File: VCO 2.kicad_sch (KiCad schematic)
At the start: 99 parts, among them J1 OUT 1x4s, J16 OCT_SW 1x7s, J18 CV 1x6s, J8 CTRL 1x8s, J85 Eurorack 2x8hs, J9 IN 1x6s, Q1 2N3904, Q2 2N3904, U1 CEM3340, U2 TL074, U3 TL074, U4 LM336Z-2.5/LFT3

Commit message: Moved LED to control board.
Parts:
- removed D1: LED, symbol Device:LED
- added J20: LED 1x2s, symbol Connector:Conn_01x02_Socket
- R51: value 470R -> 470R/520R
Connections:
- net +12V: no longer C18.1, C20.1, R73.1
- net at R51.1: now also J20.2 (Pin_2)
- new net: C18.1, C20.1, J20.1 (Pin_1), R73.1
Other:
- note added: "3.1V/2.1V"
- note added: "Based on the Thomas Henry sine wave shaper"
- note added: "Needs to be precise"
- note removed: "This is the sine wave generator"
- moved on the sheet: C4, C5, C7, C8, R51, TP22, U2E, U3E

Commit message: Updated TP names
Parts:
- TP2: value SQR -> Sqr
- TP3: value SAW -> Saw
- TP4: value TRI -> Tri
- TP5: value SIN -> Sine
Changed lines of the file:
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@@
 			)
 		)
-		(property "Value" "SAW"
+		(property "Value" "Saw"
 			(at 146.05 51.3079 0)
 			(effects
@@
 			)
 		)
-		(property "Value" "SIN"
+		(property "Value" "Sine"
 			(at 308.61 49.0221 0)
 			(effects
@@
 			)
 		)
-		(property "Value" "TRI"
+		(property "Value" "Tri"
 			(at 147.32 80.5179 0)
 			(effects
@@
 			)
 		)
-		(property "Value" "SQR"
+		(property "Value" "Sqr"
 			(at 146.05 27.1779 0)
 			(effects

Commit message: Added fp and moved controls
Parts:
- C1: value 10nF -> 10nF f; footprint Capacitor_THT:C_Disc_D4.7mm_W2.5mm_P5.00mm -> Capacitor_THT:C_Rect_L7.2mm_W2.5mm_P5.00mm
- C10, C11: value 100nF -> 100nF f; footprint Capacitor_THT:C_Disc_D4.7mm_W2.5mm_P5.00mm -> Capacitor_THT:C_Rect_L7.2mm_W2.5mm_P5.00mm
- C12, C20, C21, C4, C5, C7, C8: value 0.1μF -> 0.1μF c
- C13: value 1nF -> 1nF f; footprint (none) -> Capacitor_THT:C_Rect_L7.2mm_W2.5mm_P5.00mm
- C14: value 10uF -> 10uF c; footprint (none) -> Capacitor_THT:C_Disc_D4.7mm_W2.5mm_P5.00mm
- C18, C19: value 47μF -> 47μF e
- C2: value 10μF -> 10μF c
- C3: value 100nF -> 100nF c
- C6: value 1000pF -> 1000pF f; footprint Capacitor_THT:C_Disc_D4.7mm_W2.5mm_P5.00mm -> Capacitor_THT:C_Rect_L7.2mm_W2.5mm_P5.00mm
- C9: value 1nF -> 1nF f; footprint Capacitor_THT:C_Disc_D4.7mm_W2.5mm_P5.00mm -> Capacitor_THT:C_Rect_L7.2mm_W2.5mm_P5.00mm
- H1, H2, H3, H4: value ~ -> (none)
- J20: footprint (none) -> Connector_PinSocket_2.54mm:PinSocket_1x02_P2.54mm_Vertical
- J8: footprint (none) -> Connector_PinSocket_2.54mm:PinSocket_1x08_P2.54mm_Vertical
- R17, R43, R44, R45, R46, R47, R48, R49, R50, R51: footprint (none) -> Resistor_THT:R_Axial_DIN0204_L3.6mm_D1.6mm_P7.62mm_Horizontal
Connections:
- net +12V: now also C18.1, C20.1, J20.1 (Pin_1), R73.1
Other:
- added sheet Front Panel (front_panel.kicad_sch)
- sheet Controls: file untitled.kicad_sch -> controls.kicad_sch

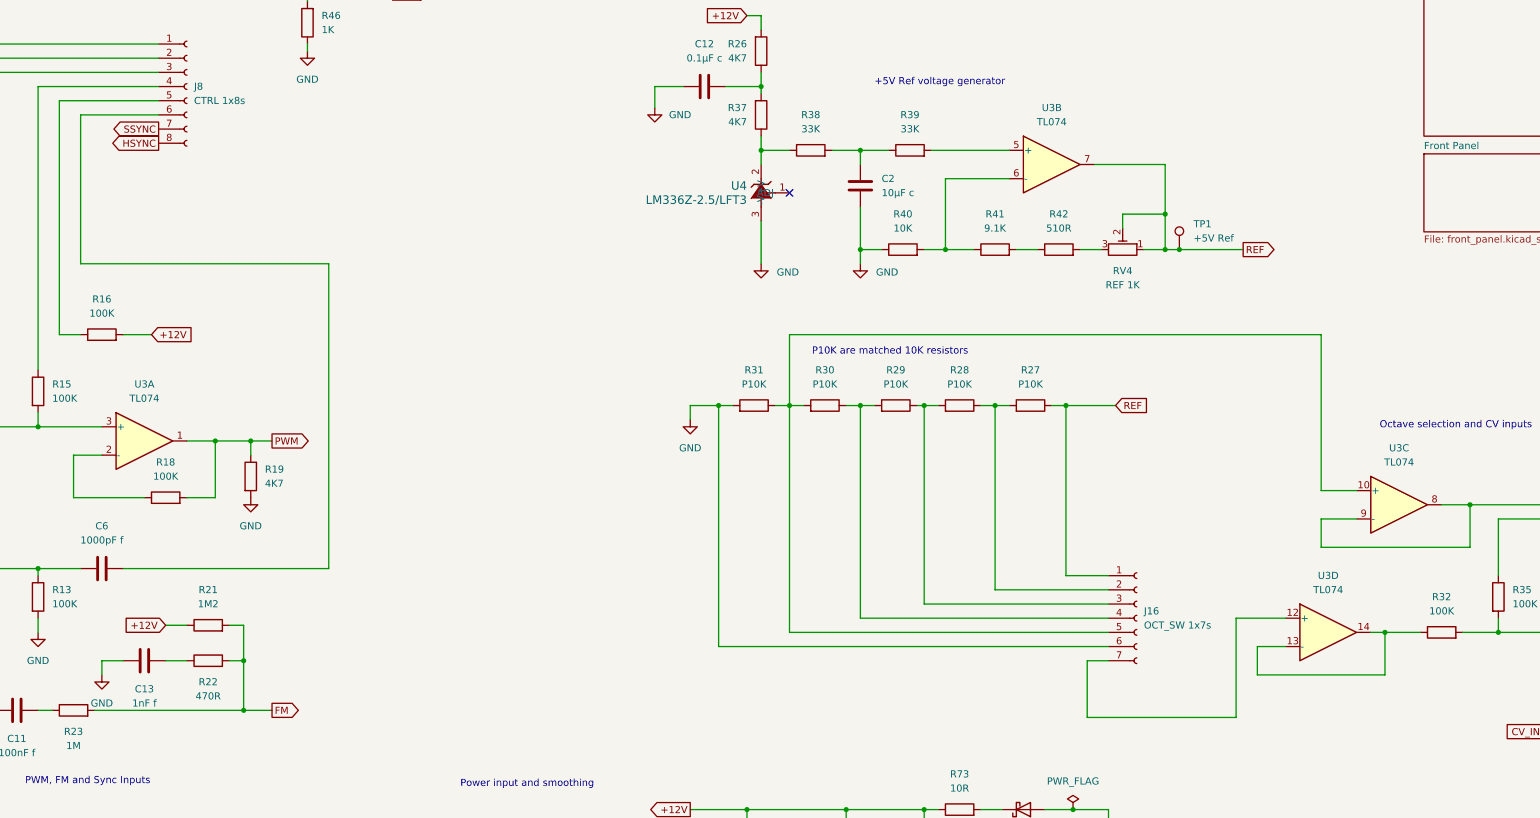
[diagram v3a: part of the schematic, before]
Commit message: Designed PCB and generated JLCPCB files
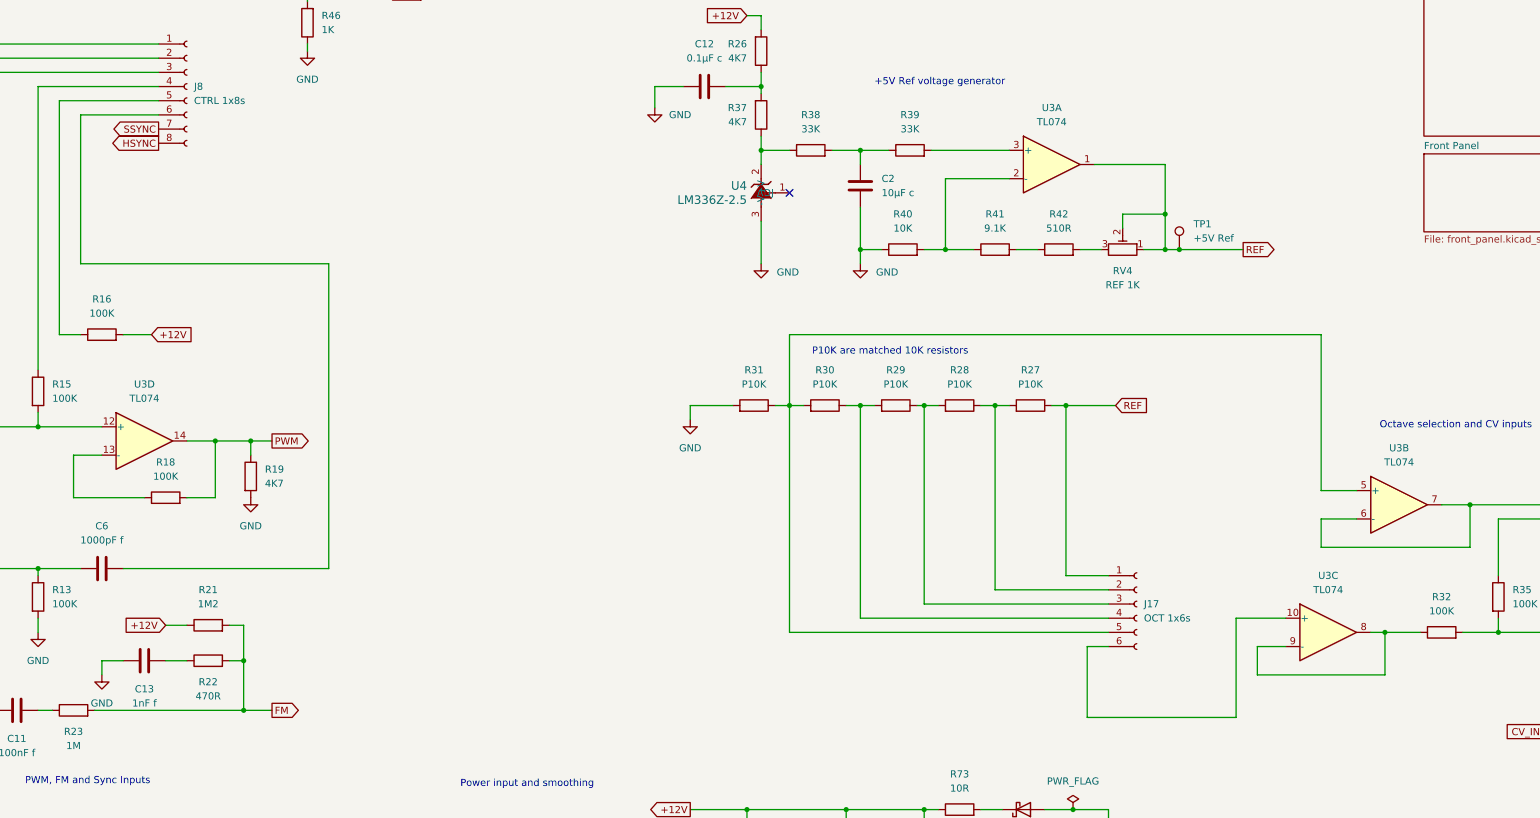
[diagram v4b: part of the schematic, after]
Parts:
- removed J16: OCT_SW 1x7s, Connector_PinSocket_2.54mm:PinSocket_1x07_P2.54mm_Vertical, symbol Connector:Conn_01x07_Socket
- added J17: OCT 1x6s, Connector_PinSocket_2.54mm:PinSocket_1x06_P2.54mm_Vertical, symbol Connector:Conn_01x06_Socket
- Q1, Q2: footprint Package_TO_SOT_THT:TO-92_Inline -> Package_TO_SOT_THT:TO-92_Inline_Wide
- R10, R11, R12, R13, R14, R15, R16, R17, R18, R19, R2, R20, R21, R24, R26, R27, R28, R29, R30, R31, R33, R34, R35, R36, R37, R38, R39, R4, R40, R41, R42, R43, R44, R45, R46, R47, R49, R5, R50, R51, R7, R73, R74, R8, R9: footprint Resistor_THT:R_Axial_DIN0204_L3.6mm_D1.6mm_P7.62mm_Horizontal -> Resistor_THT:R_Axial_DIN0204_L3.6mm_D1.6mm_P2.54mm_Vertical
- U4: value LM336Z-2.5/LFT3 -> LM336Z-2.5
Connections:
- net PWM: now also U3.14; no longer U3.1
- net REF: now also U3.1, J17.1 (Pin_1); no longer U3.7
- net at R39.2: now also U3.3 (+); no longer U3.5 (+)
- net at R40.2, R41.1: now also U3.2 (-); no longer U3.6 (-)
- net at R30.2, R31.1: now also U3.5 (+), J17.5 (Pin_5); no longer U3.10 (+)
- net at U3.8, U3.9 (-): now also R32.1; no longer J18.1 (Pin_1)
- net at R28.2, R29.1: now also J17.3 (Pin_3)
- net at R29.2, R30.1: now also J17.4 (Pin_4)
- net at R27.2, R28.1: now also J17.2 (Pin_2)
- net at U3.12 (+): now also R14.2, R15.2
- net at R18.1: now also U3.13 (-); no longer U3.2 (-)
- new net: J18.1 (Pin_1), U3.6 (-), U3.7
- new net: J17.6 (Pin_6), U3.10 (+)

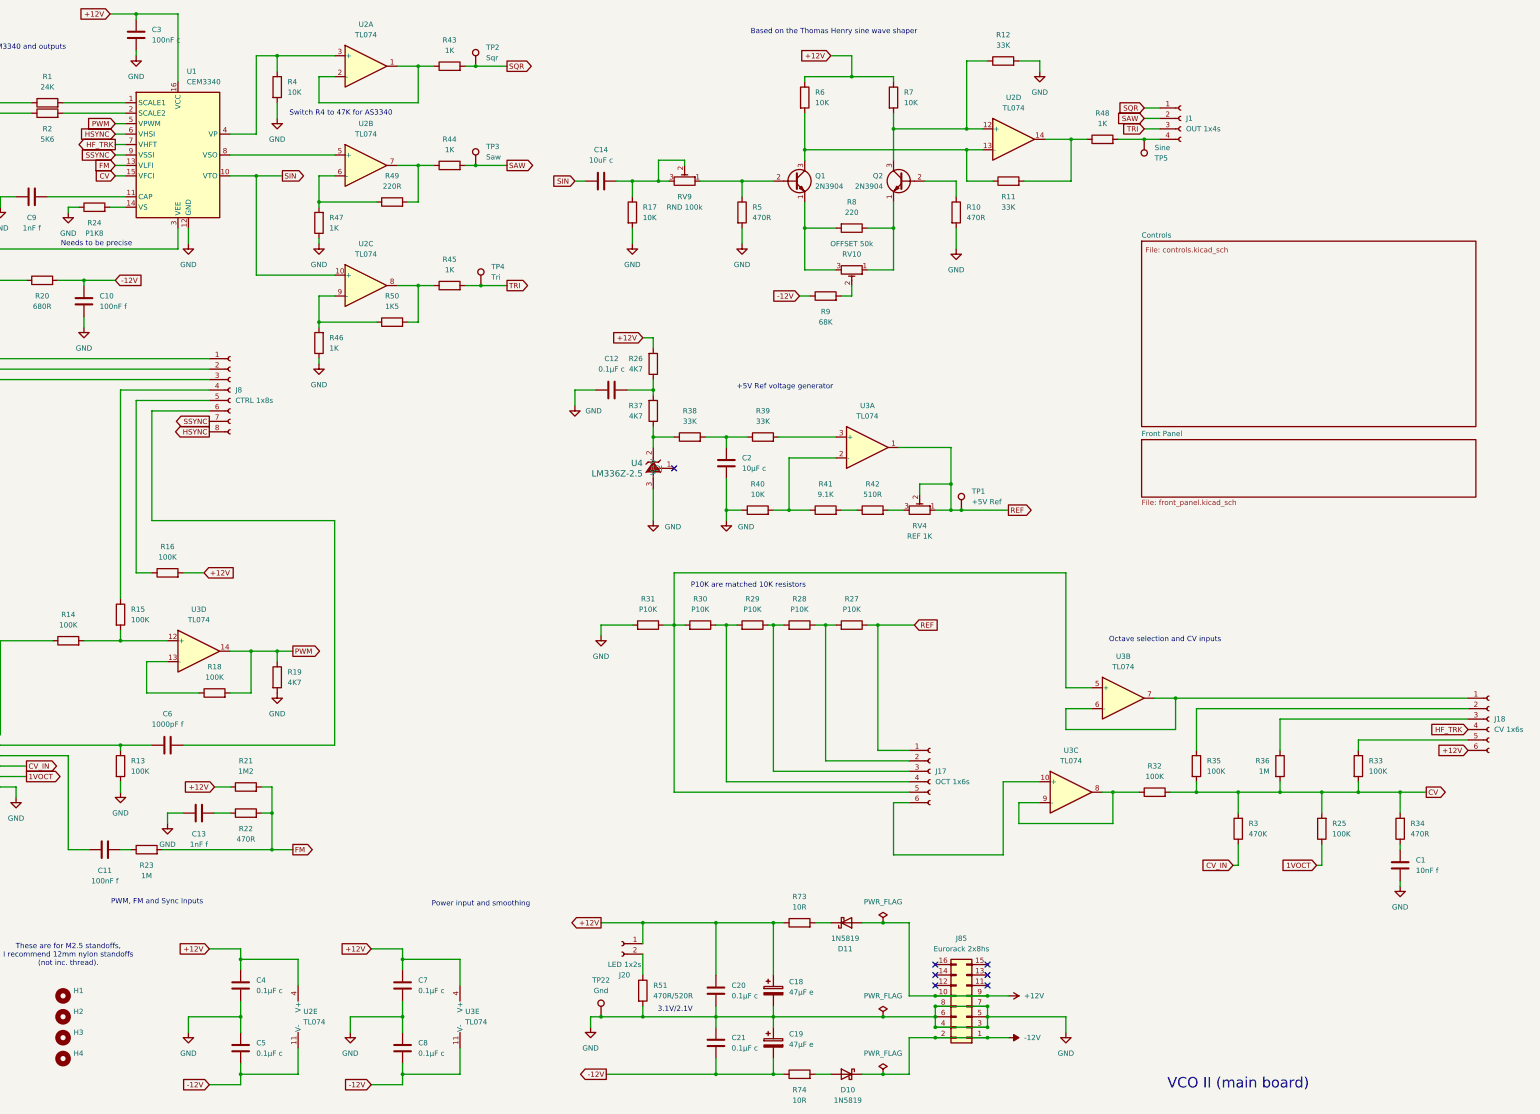
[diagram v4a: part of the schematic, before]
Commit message: Fixed switches, added new FPs and symbols.
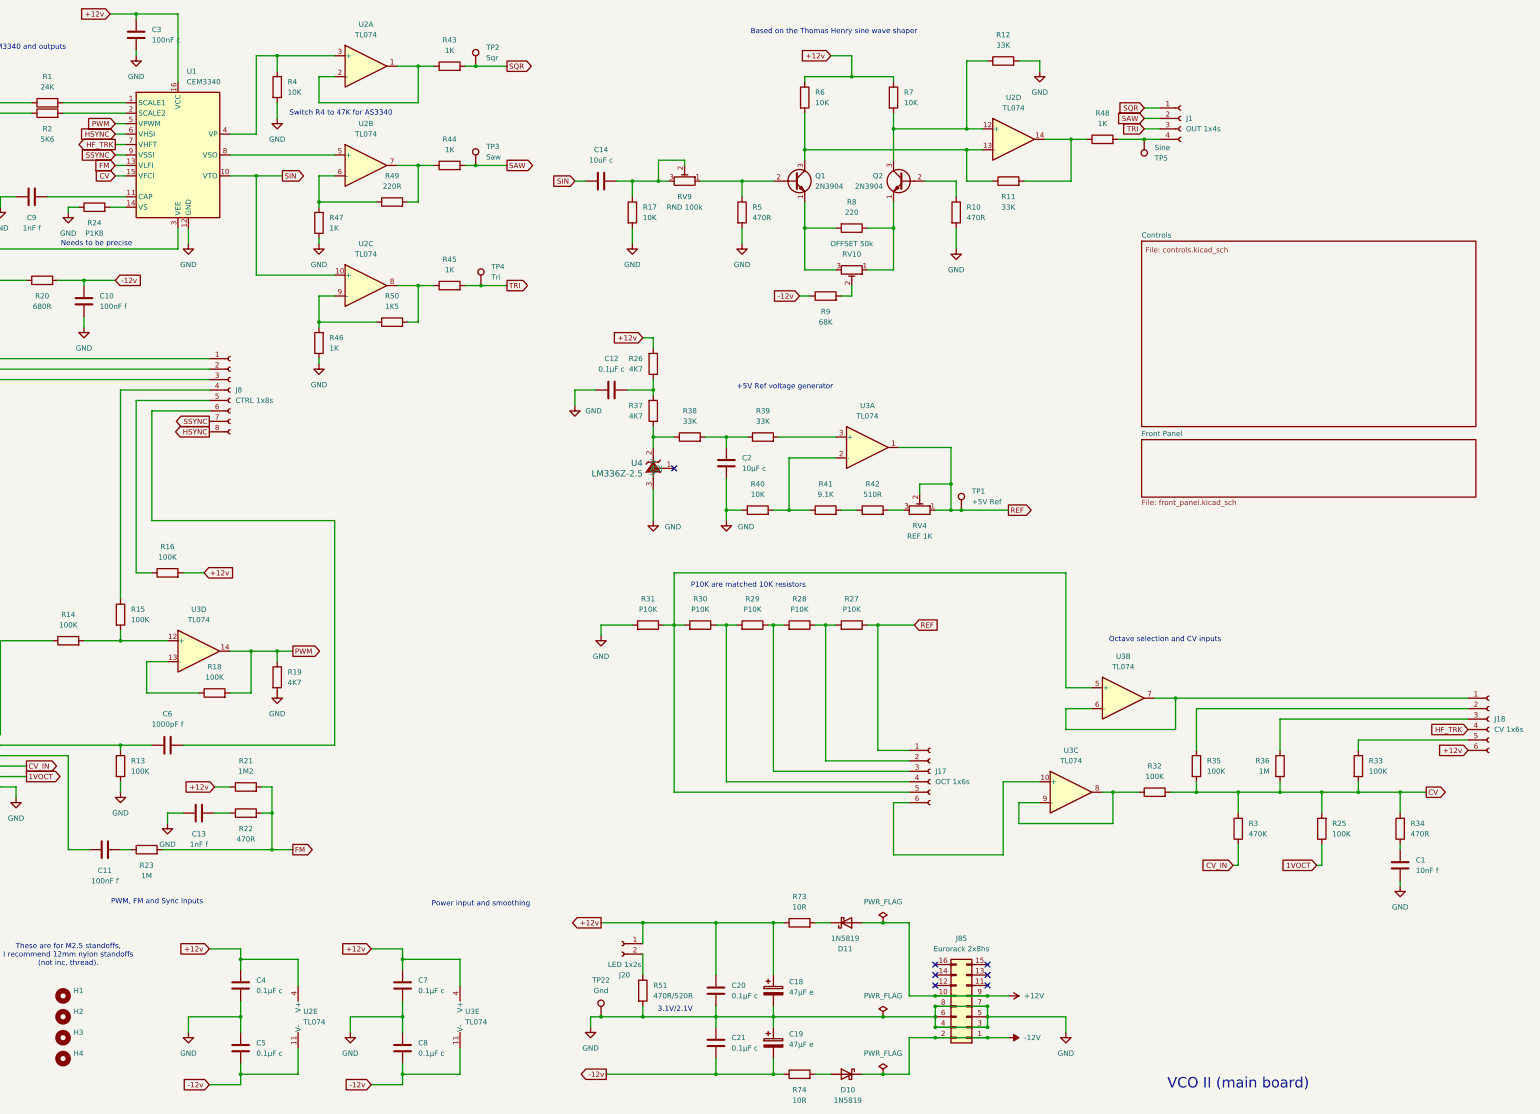
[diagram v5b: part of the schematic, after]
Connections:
- net +12V: no longer C18.1, C20.1, C3.1, C4.1, C7.1, J18.6 (Pin_6), J20.1 (Pin_1), R16.2, R21.1, R26.2, R6.1, R7.1, R73.1, U1.16 (VCC), U2.4 (V+), U3.4 (V+)
- net -12V: no longer C10.2, C19.2, C21.2, C5.2, C8.2, R20.2, R74.1, R9.1, U2.11 (V-), U3.11 (V-)
- new net +12v: C18.1, C20.1, C3.1, C4.1, C7.1, J18.6 (Pin_6), J20.1 (Pin_1), R16.2, R21.1, R26.2, R6.1, R7.1, R73.1, U1.16 (VCC), U2.4 (V+), U3.4 (V+)
- new net -12v: C10.2, C19.2, C21.2, C5.2, C8.2, R20.2, R74.1, R9.1, U2.11 (V-), U3.11 (V-)
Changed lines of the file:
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@@
 	)
 	(junction
-		(at 191.77 165.1)
-		(diameter 0)
-		(color 0 0 0 0)
-	)
-	(junction
 		(at 129.54 53.34)
 		(diameter 0)
@@
 	)
 	(junction
+		(at 191.77 165.1)
+		(diameter 0)
+		(color 0 0 0 0)
+	)
+	(junction
 		(at 105.41 62.23)
 		(diameter 0)
@@
 	(wire
 		(pts
+			(xy 191.77 165.1) (xy 194.31 165.1)
+		)
+		(stroke
+			(width 0)
+			(type default)
+		)
+	)
+	(wire
+		(pts
 			(xy 95.25 26.67) (xy 95.25 30.48)
 		)
@@
 	(wire
 		(pts
-			(xy 194.31 165.1) (xy 191.77 165.1)
-		)
-		(stroke
-			(width 0)
-			(type default)
-		)
-	)
-	(wire
-		(pts
 			(xy 60.96 152.4) (xy 64.77 152.4)
 		)
@@
 		)
 	)
-	(global_label "-12V"
+	(global_label "-12v"
 		(shape input)
 		(at 118.11 276.86 180)
@@
 		)
 	)
-	(global_label "-12V"
+	(global_label "-12v"
 		(shape input)
 		(at 78.74 276.86 180)
@@
 		)
 	)
-	(global_label "-12V"
+	(global_label "-12v"
 		(shape output)
 		(at 175.26 274.32 180)
@@
 		)
 	)
-	(global_label "+12V"
+	(global_label "+12v"
 		(shape input)
 		(at 118.11 243.84 180)
@@
 		)
 	)
-	(global_label "+12V"
+	(global_label "+12v"
 		(shape input)
 		(at 184.15 95.25 180)
@@
 		)
 	)
-	(global_label "+12V"
+	(global_label "+12v"
 		(shape output)
 		(at 173.99 237.49 180)
@@
 		)
 	)
-	(global_label "+12V"
+	(global_label "+12v"
 		(shape input)
 		(at 78.74 243.84 180)
@@
 		)
 	)
-	(global_label "-12V"
+	(global_label "-12v"
 		(shape input)
 		(at 55.88 81.28 0)
@@
 		)
 	)
-	(global_label "+12V"
+	(global_label "+12v"
 		(shape input)
 		(at 384.81 195.58 180)
@@
 		)
 	)
-	(global_label "-12V"
+	(global_label "-12v"
 		(shape input)
 		(at 222.25 85.09 180)
@@
 		)
 	)
-	(global_label "+12V"
+	(global_label "+12v"
 		(shape input)
 		(at 54.61 16.51 180)
@@
 		)
 	)
-	(global_label "+12V"
+	(global_label "+12v"
 		(shape input)
 		(at 80.01 204.47 180)
@@
 		)
 	)
-	(global_label "+12V"
+	(global_label "+12v"
 		(shape input)
 		(at 77.47 152.4 0)
@@
 		)
 	)
-	(global_label "+12V"
+	(global_label "+12v"
 		(shape input)
 		(at 229.87 26.67 180)

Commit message: Updates for BOM
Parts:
- R41: value 9.1K -> 9K1
- R8: value 220 -> 220R
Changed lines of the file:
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@@
 			)
 		)
-		(property "Value" "9.1K"
+		(property "Value" "9K1"
 			(at 228.6 133.35 90)
 			(show_name no)
@@
 			)
 		)
-		(property "Value" "220"
+		(property "Value" "220R"
 			(at 234.95 64.77 90)
 			(show_name no)
@@
 			(effects
 				(font
+					(face "KiCad Font")
 					(size 1.27 1.27)
 				)

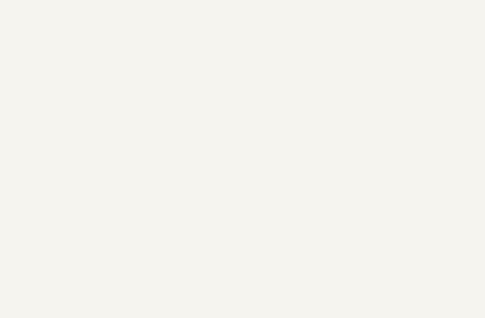
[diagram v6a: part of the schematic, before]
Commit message: Corrected connections for levels and octave switch
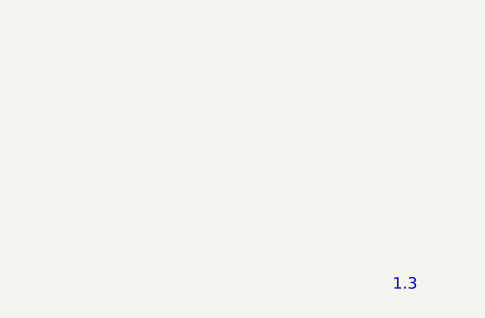
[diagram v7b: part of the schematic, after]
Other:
- note added: "1.3"
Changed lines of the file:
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@@
+		)
+	)
+	(text "1.3"
+		(exclude_from_sim no)
+		(at 393.446 280.416 0)
+		(effects
+			(font
+				(size 1.27 1.27)
+			)
 		)
 	)
